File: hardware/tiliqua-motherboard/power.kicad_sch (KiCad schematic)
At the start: 23 parts, among them J6 CONN 2x5 P=2.54mm, U5 AP63200WU

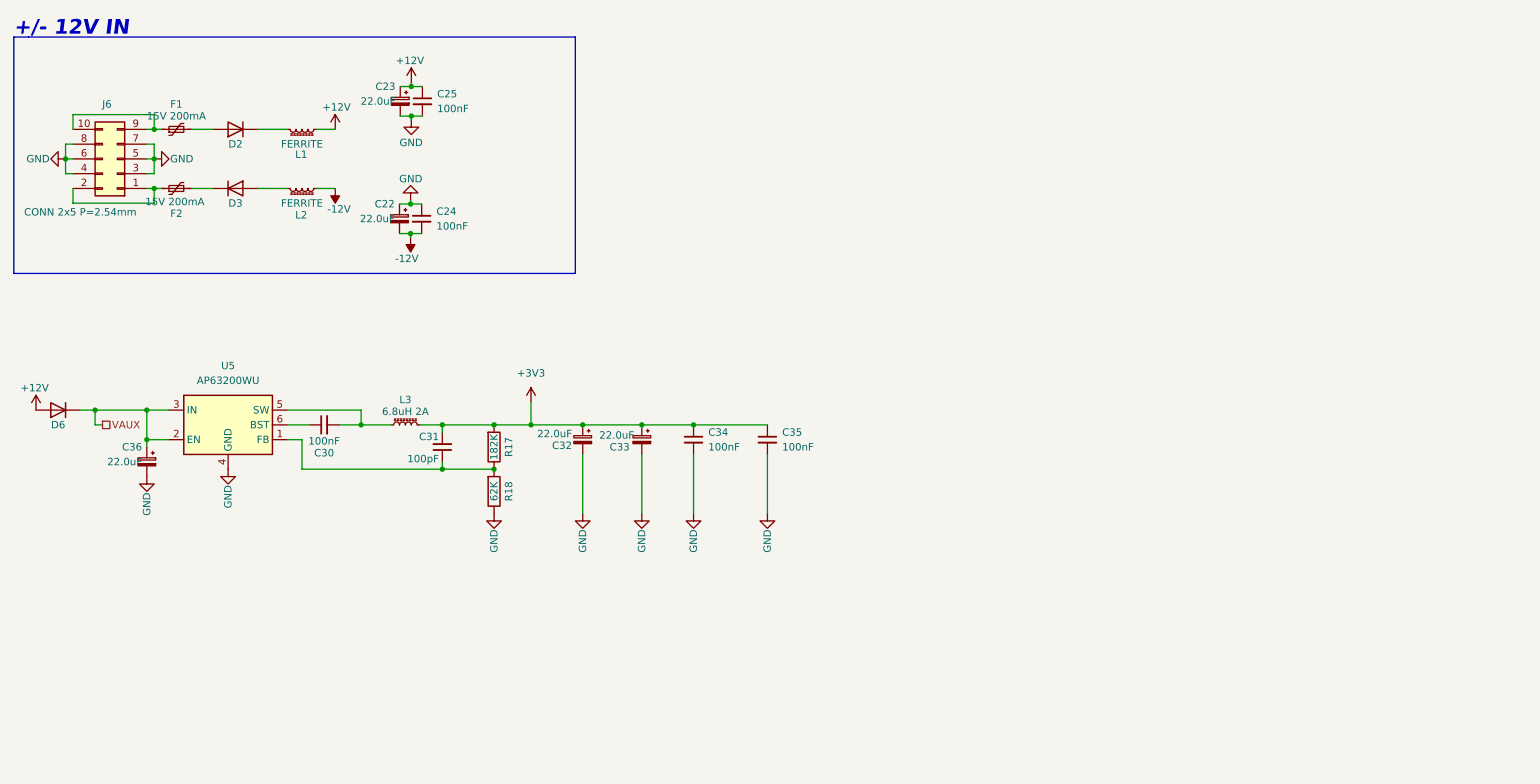
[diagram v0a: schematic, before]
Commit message: hardware/r2: squash in all changes for tiliqua R2 (#17)
* squash in all changes for Tiliqua R2
* add schematics for all components of Tiliqua R2
* update README and add lightbox photos
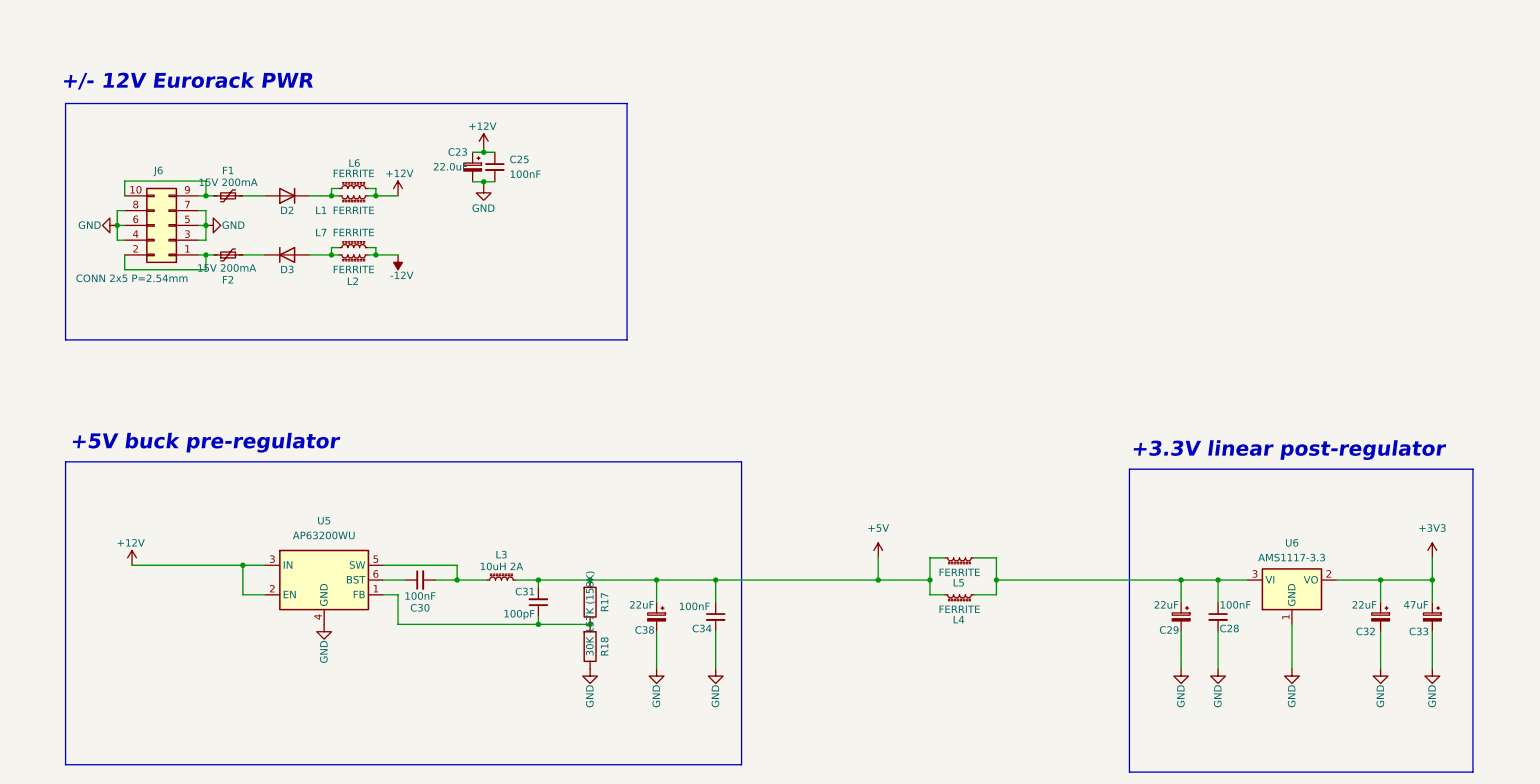
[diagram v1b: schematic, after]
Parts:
- removed C22, C36: 22.0uF, Capacitor_Tantalum_SMD:CP_EIA-3216-10_Kemet-I, symbol Device:C_Polarized_Small
- removed C24, C35: 100nF, Capacitor_SMD:C_0603_1608Metric, symbol Device:C_Small
- removed D6: 1N4007FL, Diode_SMD:D_SOD-123F, symbol Diode:US1G
- added C28: 100nF, Capacitor_SMD:C_0603_1608Metric, symbol Device:C_Small
- added C29, C38: 22uF, Capacitor_Tantalum_SMD:CP_EIA-3216-10_Kemet-I, symbol Device:C_Polarized_Small
- added L4, L5, L6, L7: FERRITE, Inductor_SMD:L_0603_1608Metric, symbol Device:L_Ferrite_Small
- added U6: AMS1117-3.3, Package_TO_SOT_SMD:SOT-223-3_TabPin2, symbol Regulator_Linear:AMS1117-3.3
- C32: value 22.0uF -> 22uF
- C33: value 22.0uF -> 47uF; footprint Capacitor_Tantalum_SMD:CP_EIA-3216-10_Kemet-I -> Capacitor_SMD:CP_Elec_6.3x5.4; lcsc# C782264 -> C88735; mfg# CA45-A-16V-22uF-K -> 25SEV47M6.3X5.5
- L3: value 6.8uH 2A -> 10uH 2A; lcsc# C844992 -> C844996
- R17: value 182K -> 157K (158K); PN RC0402FR-074K7L -> (none); lcsc# C327365 -> C861679
- R18: value 62K -> 30K; PN RC0402FR-074K7L -> (none); lcsc# C137950 -> C25776
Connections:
- net VAUX is gone; now on net +12V: U5.2 (EN), U5.3 (IN)
- net +12V: now also L6.2
- net +3V3: now also U6.2 (VO); no longer C31.2, C34.1, L3.2, R17.2
- net -12V: now also L7.2
- net GND: now also C28.2, C29.2, C38.2, U6.1 (GND)
- net at D3.2 (A), L2.2: now also L7.1
- net at D2.1 (K), L1.2: now also L6.1
- new net: C28.1, C29.1, L4.1, L5.1, U6.3 (VI)
- new net +5V: C31.2, C34.1, C38.1, L3.2, L4.2, L5.2, R17.2
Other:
- note added: "+/- 12V Eurorack PWR"
- note added: "+3.3V linear post-regulator"
- note added: "+5V buck pre-regulator"
- note removed: "+/- 12V IN"
- moved on the sheet: C23, C25, C30, C31, C34, D2, D3, F1, F2, J6, L1, L2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
